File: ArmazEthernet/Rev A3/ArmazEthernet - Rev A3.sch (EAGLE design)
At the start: 121 parts, among them J1 22-05-7028-02, P1 RB1-125BAG1A, T1 H1102FNL, T2 H1102FNL, U1 TC1264-3.3, U2 TC1264-1.8, U3 KSZ8995MA, U4 AT24C02C-SSHM-B, X1 NE8FAV, X2 NE8FAV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

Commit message: Put the LED of Neutrik connectors on pull-down
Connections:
- net +3V3: now also R41.2, R42.2, R43.2, R44.2
- net GND: no longer LED4.C, LED5.C, LED6.C, LED7.C
- net L1-1: now also LED4.C; no longer R41.2
- net L1-2: now also LED5.C; no longer R42.2
- net L2-1: now also LED6.C; no longer R43.2
- net L2-2: now also LED7.C; no longer R44.2
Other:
- moved on the sheet: LED4, LED5, R41, R42
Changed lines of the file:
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@@
 <attribute name="OC_NEWARK" value="86T3505"/>
 </part>
-<part name="GND34" library="supply1" deviceset="GND" device=""/>
-<part name="GND35" library="supply1" deviceset="GND" device=""/>
-<part name="GND36" library="supply1" deviceset="GND" device=""/>
-<part name="GND37" library="supply1" deviceset="GND" device=""/>
 <part name="U$5" library="exmachina" deviceset="EXMACHINA-LOGO" device="-NAME">
 <attribute name="MF" value=""/>
@@
 <attribute name="OC_NEWARK" value="unknown"/>
 </part>
+<part name="+3V10" library="supply1" deviceset="+3V3" device=""/>
+<part name="+3V11" library="supply1" deviceset="+3V3" device=""/>
 </parts>
 <sheets>
@@
 <attribute name="MPN" x="35.56" y="165.1" size="1.778" layer="96" display="off"/>
 </instance>
-<instance part="LED4" gate="G$1" x="233.68" y="111.76">
-<attribute name="OC_NEWARK" x="233.68" y="111.76" size="1.778" layer="96" display="off"/>
-<attribute name="MF" x="233.68" y="111.76" size="1.778" layer="96" display="off"/>
-<attribute name="MPN" x="233.68" y="111.76" size="1.778" layer="96" display="off"/>
-</instance>
-<instance part="R41" gate="G$1" x="233.68" y="121.92" rot="R90">
-<attribute name="OC_NEWARK" x="233.68" y="121.92" size="1.778" layer="96" display="off"/>
-<attribute name="MF" x="233.68" y="121.92" size="1.778" layer="96" display="off"/>
-<attribute name="MPN" x="233.68" y="121.92" size="1.778" layer="96" display="off"/>
-</instance>
-<instance part="LED5" gate="G$1" x="243.84" y="111.76">
-<attribute name="OC_NEWARK" x="243.84" y="111.76" size="1.778" layer="96" display="off"/>
-<attribute name="MF" x="243.84" y="111.76" size="1.778" layer="96" display="off"/>
-<attribute name="MPN" x="243.84" y="111.76" size="1.778" layer="96" display="off"/>
-</instance>
-<instance part="R42" gate="G$1" x="243.84" y="121.92" rot="R90">
-<attribute name="OC_NEWARK" x="243.84" y="121.92" size="1.778" layer="96" display="off"/>
-<attribute name="MF" x="243.84" y="121.92" size="1.778" layer="96" display="off"/>
-<attribute name="MPN" x="243.84" y="121.92" size="1.778" layer="96" display="off"/>
+<instance part="LED4" gate="G$1" x="233.68" y="104.14">
+<attribute name="OC_NEWARK" x="233.68" y="104.14" size="1.778" layer="96" display="off"/>
+<attribute name="MF" x="233.68" y="104.14" size="1.778" layer="96" display="off"/>
+<attribute name="MPN" x="233.68" y="104.14" size="1.778" layer="96" display="off"/>
+</instance>
+<instance part="R41" gate="G$1" x="233.68" y="114.3" rot="R90">
+<attribute name="OC_NEWARK" x="233.68" y="114.3" size="1.778" layer="96" display="off"/>
+<attribute name="MF" x="233.68" y="114.3" size="1.778" layer="96" display="off"/>
+<attribute name="MPN" x="233.68" y="114.3" size="1.778" layer="96" display="off"/>
+</instance>
+<instance part="LED5" gate="G$1" x="243.84" y="104.14">
+<attribute name="OC_NEWARK" x="243.84" y="104.14" size="1.778" layer="96" display="off"/>
+<attribute name="MF" x="243.84" y="104.14" size="1.778" layer="96" display="off"/>
+<attribute name="MPN" x="243.84" y="104.14" size="1.778" layer="96" display="off"/>
+</instance>
+<instance part="R42" gate="G$1" x="243.84" y="114.3" rot="R90">
+<attribute name="OC_NEWARK" x="243.84" y="114.3" size="1.778" layer="96" display="off"/>
+<attribute name="MF" x="243.84" y="114.3" size="1.778" layer="96" display="off"/>
+<attribute name="MPN" x="243.84" y="114.3" size="1.778" layer="96" display="off"/>
 </instance>
 <instance part="LED6" gate="G$1" x="233.68" y="48.26">
@@
 <attribute name="MPN" x="243.84" y="58.42" size="1.778" layer="96" display="off"/>
 </instance>
-<instance part="GND34" gate="1" x="233.68" y="101.6"/>
-<instance part="GND35" gate="1" x="243.84" y="101.6"/>
-<instance part="GND36" gate="1" x="243.84" y="38.1"/>
-<instance part="GND37" gate="1" x="233.68" y="38.1"/>
 <instance part="U$5" gate="G$1" x="314.96" y="19.05">
 <attribute name="OC_NEWARK" x="314.96" y="19.05" size="1.778" layer="96" display="off"/>
@@
 <attribute name="MPN" x="246.38" y="246.38" size="1.778" layer="96" display="off"/>
 </instance>
+<instance part="+3V10" gate="G$1" x="233.68" y="127" rot="MR0"/>
+<instance part="+3V11" gate="G$1" x="233.68" y="71.12" rot="MR0"/>
 </instances>
 <busses>
@@
 <wire x1="246.38" y1="241.3" x2="246.38" y2="243.84" width="0.1524" layer="91"/>
 <junction x="246.38" y="241.3"/>
+</segment>
+<segment>
+<pinref part="R41" gate="G$1" pin="2"/>
+<pinref part="+3V10" gate="G$1" pin="+3V3"/>
+<wire x1="233.68" y1="119.38" x2="233.68" y2="121.92" width="0.1524" layer="91"/>
+<pinref part="R42" gate="G$1" pin="2"/>
+<wire x1="233.68" y1="121.92" x2="233.68" y2="124.46" width="0.1524" layer="91"/>
+<wire x1="233.68" y1="121.92" x2="243.84" y2="121.92" width="0.1524" layer="91"/>
+<wire x1="243.84" y1="121.92" x2="243.84" y2="119.38" width="0.1524" layer="91"/>
+<junction x="233.68" y="121.92"/>
+</segment>
+<segment>
+<pinref part="R43" gate="G$1" pin="2"/>
+<pinref part="+3V11" gate="G$1" pin="+3V3"/>
+<wire x1="233.68" y1="63.5" x2="233.68" y2="66.04" width="0.1524" layer="91"/>
+<pinref part="R44" gate="G$1" pin="2"/>
+<wire x1="233.68" y1="66.04" x2="233.68" y2="68.58" width="0.1524" layer="91"/>
+<wire x1="243.84" y1="63.5" x2="243.84" y2="66.04" width="0.1524" layer="91"/>
+<wire x1="243.84" y1="66.04" x2="233.68" y2="66.04" width="0.1524" layer="91"/>
+<junction x="233.68" y="66.04"/>
 </segment>
 </net>
@@
 </segment>
 <segment>
-<pinref part="GND37" gate="1" pin="GND"/>
-<pinref part="LED6" gate="G$1" pin="C"/>
-<wire x1="233.68" y1="40.64" x2="233.68" y2="43.18" width="0.1524" layer="91"/>
-</segment>
-<segment>
-<pinref part="GND36" gate="1" pin="GND"/>
-<pinref part="LED7" gate="G$1" pin="C"/>
-<wire x1="243.84" y1="40.64" x2="243.84" y2="43.18" width="0.1524" layer="91"/>
-</segment>
-<segment>
-<pinref part="GND34" gate="1" pin="GND"/>
-<pinref part="LED4" gate="G$1" pin="C"/>
-<wire x1="233.68" y1="104.14" x2="233.68" y2="106.68" width="0.1524" layer="91"/>
-</segment>
-<segment>
-<pinref part="GND35" gate="1" pin="GND"/>
-<pinref part="LED5" gate="G$1" pin="C"/>
-<wire x1="243.84" y1="104.14" x2="243.84" y2="106.68" width="0.1524" layer="91"/>
-</segment>
-<segment>
 <pinref part="JP2" gate="A" pin="8"/>
 <pinref part="GND30" gate="1" pin="GND"/>
@@
 </segment>
 <segment>
-<pinref part="R42" gate="G$1" pin="2"/>
-<wire x1="243.84" y1="127" x2="243.84" y2="129.54" width="0.1524" layer="91"/>
-<wire x1="243.84" y1="129.54" x2="246.38" y2="129.54" width="0.1524" layer="91"/>
-<label x="246.38" y="129.54" size="1.27" layer="95" xref="yes"/>
+<wire x1="243.84" y1="91.44" x2="246.38" y2="91.44" width="0.1524" layer="91"/>
+<pinref part="LED5" gate="G$1" pin="C"/>
+<wire x1="243.84" y1="91.44" x2="243.84" y2="99.06" width="0.1524" layer="91"/>
+<label x="246.38" y="91.44" size="1.27" layer="95" xref="yes"/>
 </segment>
 </net>
@@
 </segment>
 <segment>
-<pinref part="R41" gate="G$1" pin="2"/>
-<wire x1="233.68" y1="127" x2="233.68" y2="132.08" width="0.1524" layer="91"/>
-<wire x1="233.68" y1="132.08" x2="246.38" y2="132.08" width="0.1524" layer="91"/>
-<label x="246.38" y="132.08" size="1.27" layer="95" xref="yes"/>
+<wire x1="233.68" y1="88.9" x2="246.38" y2="88.9" width="0.1524" layer="91"/>
+<pinref part="LED4" gate="G$1" pin="C"/>
+<wire x1="233.68" y1="99.06" x2="233.68" y2="88.9" width="0.1524" layer="91"/>
+<label x="246.38" y="88.9" size="1.27" layer="95" xref="yes"/>
 </segment>
 </net>
 <net name="L2-2" class="0">
-<segment>
-<pinref part="R44" gate="G$1" pin="2"/>
-<wire x1="243.84" y1="63.5" x2="243.84" y2="66.04" width="0.1524" layer="91"/>
-<wire x1="243.84" y1="66.04" x2="248.92" y2="66.04" width="0.1524" layer="91"/>
-<label x="248.92" y="66.04" size="1.27" layer="95" xref="yes"/>
-</segment>
 <segment>
 <pinref part="JP5" gate="A" pin="7"/>
@@
 <junction x="345.44" y="175.26"/>
 </segment>
+<segment>
+<wire x1="243.84" y1="35.56" x2="248.92" y2="35.56" width="0.1524" layer="91"/>
+<pinref part="LED7" gate="G$1" pin="C"/>
+<wire x1="243.84" y1="35.56" x2="243.84" y2="43.18" width="0.1524" layer="91"/>
+<label x="248.92" y="35.56" size="1.27" layer="95" xref="yes"/>
+</segment>
 </net>
 <net name="L2-1" class="0">
-<segment>
-<pinref part="R43" gate="G$1" pin="2"/>
-<wire x1="233.68" y1="63.5" x2="233.68" y2="68.58" width="0.1524" layer="91"/>
-<wire x1="233.68" y1="68.58" x2="248.92" y2="68.58" width="0.1524" layer="91"/>
-<label x="248.92" y="68.58" size="1.27" layer="95" xref="yes"/>
-</segment>
 <segment>
 <pinref part="JP4" gate="A" pin="6"/>
@@
 <junction x="347.98" y="177.8"/>
 </segment>
+<segment>
+<wire x1="233.68" y1="33.02" x2="248.92" y2="33.02" width="0.1524" layer="91"/>
+<pinref part="LED6" gate="G$1" pin="C"/>
+<wire x1="233.68" y1="33.02" x2="233.68" y2="43.18" width="0.1524" layer="91"/>
+<label x="248.92" y="33.02" size="1.27" layer="95" xref="yes"/>
+</segment>
 </net>
 <net name="N$20" class="0">
@@
 <pinref part="LED4" gate="G$1" pin="A"/>
 <pinref part="R41" gate="G$1" pin="1"/>
-<wire x1="233.68" y1="114.3" x2="233.68" y2="116.84" width="0.1524" layer="91"/>
+<wire x1="233.68" y1="106.68" x2="233.68" y2="109.22" width="0.1524" layer="91"/>
 </segment>
 </net>
@@
 <pinref part="LED5" gate="G$1" pin="A"/>
 <pinref part="R42" gate="G$1" pin="1"/>
-<wire x1="243.84" y1="114.3" x2="243.84" y2="116.84" width="0.1524" layer="91"/>
-</segment>
-</net>
+<wire x1="243.84" y1="106.68" x2="243.84" y2="109.22" width="0.1524" layer="91"/>
+</segment>
+</net>

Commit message: Change CC-BY-NC-SA logo on the board ArmazEthernet Rev A3
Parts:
- removed U$6: CC-BY-SA, cc-by-sa:CC-BY-SA
- added U$7: CC-BY-NC-SA, cc-by-sa:CC-BY-NC-SA
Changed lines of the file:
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@@
-<attribute name="OC_NEWARK" value="unknown"/>
-</part>
-<part name="U$6" library="cc-by-sa" deviceset="CC-BY-SA" device="">
-<attribute name="MF" value=""/>
-<attribute name="MPN" value=""/>
 <attribute name="OC_NEWARK" value="unknown"/>
 </part>
@@
 <part name="+3V10" library="supply1" deviceset="+3V3" device=""/>
 <part name="+3V11" library="supply1" deviceset="+3V3" device=""/>
+<part name="U$7" library="cc-by-sa" deviceset="CC-BY-NC-SA" device=""/>
 </parts>
 <sheets>
@@
 <attribute name="MPN" x="314.96" y="19.05" size="1.778" layer="96" display="off"/>
 </instance>
-<instance part="U$6" gate="A" x="314.96" y="8.89">
-<attribute name="OC_NEWARK" x="314.96" y="8.89" size="1.778" layer="96" display="off"/>
-<attribute name="MF" x="314.96" y="8.89" size="1.778" layer="96" display="off"/>
-<attribute name="MPN" x="314.96" y="8.89" size="1.778" layer="96" display="off"/>
-</instance>
 <instance part="R32" gate="G$1" x="340.36" y="66.04" rot="MR90">
 <attribute name="OC_NEWARK" x="340.36" y="66.04" size="1.778" layer="96" display="off"/>
@@
 <instance part="+3V10" gate="G$1" x="233.68" y="127" rot="MR0"/>
 <instance part="+3V11" gate="G$1" x="233.68" y="71.12" rot="MR0"/>
+<instance part="U$7" gate="G$1" x="307.34" y="8.89"/>
 </instances>
 <busses>

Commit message: Update the placement of the logo and add seriegraphie of the test pads
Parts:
- added U$6: CC-BY-NC-SA, cc-by-sa:CC-BY-NC-SA
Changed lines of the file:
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@@
 <part name="+3V10" library="supply1" deviceset="+3V3" device=""/>
 <part name="+3V11" library="supply1" deviceset="+3V3" device=""/>
+<part name="U$6" library="cc-by-sa" deviceset="CC-BY-NC-SA" device=""/>
 <part name="U$7" library="cc-by-sa" deviceset="CC-BY-NC-SA" device=""/>
 </parts>
@@
 <instance part="+3V10" gate="G$1" x="233.68" y="127" rot="MR0"/>
 <instance part="+3V11" gate="G$1" x="233.68" y="71.12" rot="MR0"/>
-<instance part="U$7" gate="G$1" x="307.34" y="8.89"/>
+<instance part="U$6" gate="G$1" x="307.34" y="9.144"/>
 </instances>
 <busses>
@@
 <instance part="JP9" gate="G$1" x="354.076" y="21.59"/>
 <instance part="JP10" gate="G$1" x="358.394" y="21.59"/>
+<instance part="U$7" gate="G$1" x="307.34" y="8.89"/>
 </instances>
 <busses>

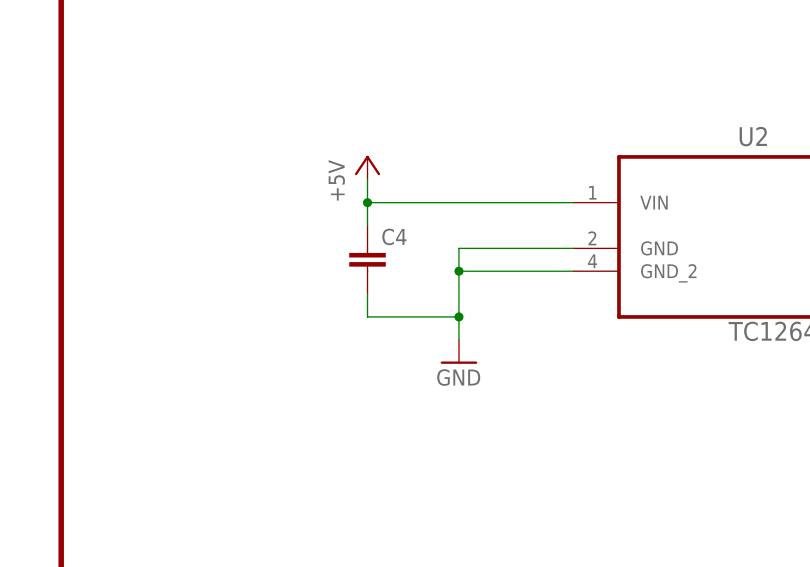
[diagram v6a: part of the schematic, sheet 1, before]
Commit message: Update attributes in ArmazEthernet - Rev A3
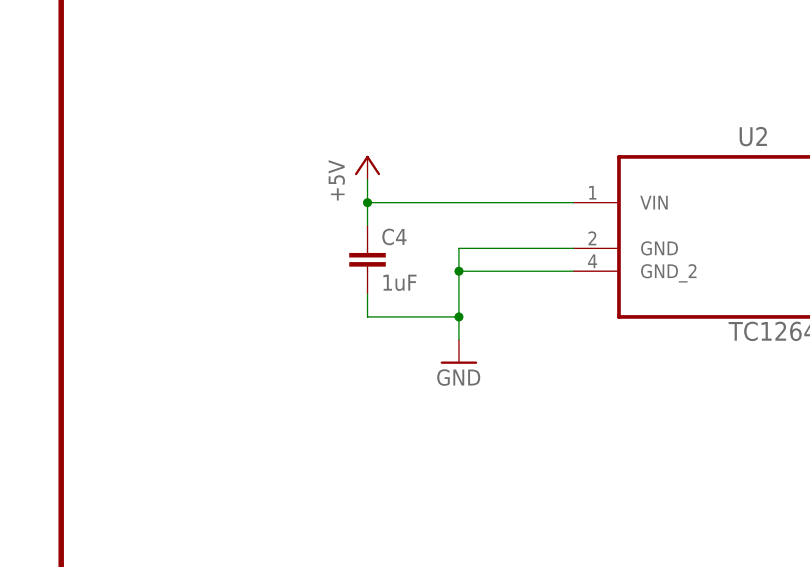
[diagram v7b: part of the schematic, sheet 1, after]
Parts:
- C1, C2, C3, JP10, JP7, JP8, JP9, P1, T1, T2, TP1, TP3, TP4, TP5, U$5, U$6, U$7, U$8, U1, U2: OC_FARNELL (none) -> unknown
- C10, C13, C14, C19, C21, C26, C27, C28, C29, C30, C31, C32, C33, C34, C35, C36, C37, C38, C39, C40, C43, C44, C9: MF (none) -> MULTICOMP; MPN MC0603B104K160CT -> MC0603B104K250CT; OC_FARNELL (none) -> 1759037
- C11, C12, C46, C47: MPN MC1206B102K202CT -> (none); OC_FARNELL (none) -> unknown
- C15, C16, C17: MPN MCCTA475M010 -> (none); OC_FARNELL (none) -> unknown
- C18, C20, C45: MF (none) -> MURATA; MPN MCNP16V106M5X11 -> GRM32DR71C106KA01L; OC_FARNELL (none) -> 2494299
- C4: value (none) -> 1uF; OC_FARNELL (none) -> unknown
- C41, C42: MF (none) -> MULTICOMP; MPN MC0603N180J500CT -> MC0603B183K160CT; OC_FARNELL (none) -> 1759006
- CR1: MF (none) -> VISHAY; MPN SMAJ33A-E3/61 -> SMAJ33A-E3/5A; OC_FARNELL (none) -> 1812505
- J1: MF (none) -> MOLEX
- JP1: MPN M20-9990545 -> (none); OC_FARNELL (none) -> unknown
- JP2, JP4: MF (none) -> SAMTEC; MPN 2211S-08G -> TSW-108-15-T-S; OC_FARNELL (none) -> 2037596
- JP3, JP5: MF (none) -> SAMTEC; MPN 2212S-08SG-85 -> SLW-108-01-T-S; OC_FARNELL (none) -> 1803516
- L3: MPN LQH43CN150K03L -> (none); OC_FARNELL (none) -> unknown
- LED1, LED2, LED3: MF (none) -> MULTICOMP; OC_FARNELL (none) -> 1716771
- LED4, LED5, LED6, LED7: MF (none) -> MULTICOMP; OC_FARNELL (none) -> 1716770
- R1, R2, R27: MF Multicomp Passives -> MULTICOMP; MPN MC0063W060311K5 -> MCMR06X1501FTL; OC_FARNELL (none) -> 2073391
- R10, R11, R12, R14, R15, R16, R17, R18, R5, R7, R8, R9: MF Multicomp Passives -> MULTICOMP; MPN MC0063W0603151R -> MCMR06X49R9FTL; OC_FARNELL (none) -> 2073520
- R13, R6: MF Multicomp Passives -> MULTICOMP; MPN MC0063W0603175R -> MCMR06X75R0FTL; OC_FARNELL (none) -> 2073571
- R19, R20, R21, R22, R23, R24, R25, R26, R32, R33, R45, R46: MF (none) -> MULTICOMP; MPN MC0603SAF499JT5E -> MCMR06X49R9FTL; OC_FARNELL (none) -> 2073520
- R30, R31: MF Multicomp Passives -> (none); MPN MC0063W0603110K -> (none); OC_FARNELL (none) -> unknown
- R34: MF (none) -> MULTICOMP; MPN MC0063W060313K01 -> MCMR06X3001FTL; OC_FARNELL (none) -> 2073461
- R35, R36, R37, R38, R39, R40: MF Multicomp Passives -> (none); MPN MC0603WG00000T5E-TC -> (none); OC_FARNELL (none) -> unknown
- R41, R42, R43, R44: MF (none) -> MULTICOMP; OC_FARNELL (none) -> 2073348
- R47, R48: MF Multicomp Passives -> MULTICOMP; MPN MC0063W06031220R -> MCMR06X2200FTL; OC_FARNELL (none) -> 2073428
- R49: MF Multicomp Passives -> MULTICOMP; MPN MC0063W0603110K -> MCMR06X1002FTL; OC_FARNELL (none) -> 2073349
- U$9: MPN 1N4148W -> (none); OC_FARNELL (none) -> unknown
- U3: MF (none) -> MICROCHIP; OC_FARNELL (none) -> 2509844
- U4: MF (none) -> ATMEL; OC_FARNELL (none) -> 1971995
- X1, X2: OC_FARNELL (none) -> 1202031
- Y1: MF (none) -> TXC; OC_FARNELL (none) -> 1842189
